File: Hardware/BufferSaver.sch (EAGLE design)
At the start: 12 parts, among them U1 SN74AHC1G125, U3 SN74AHC1G125

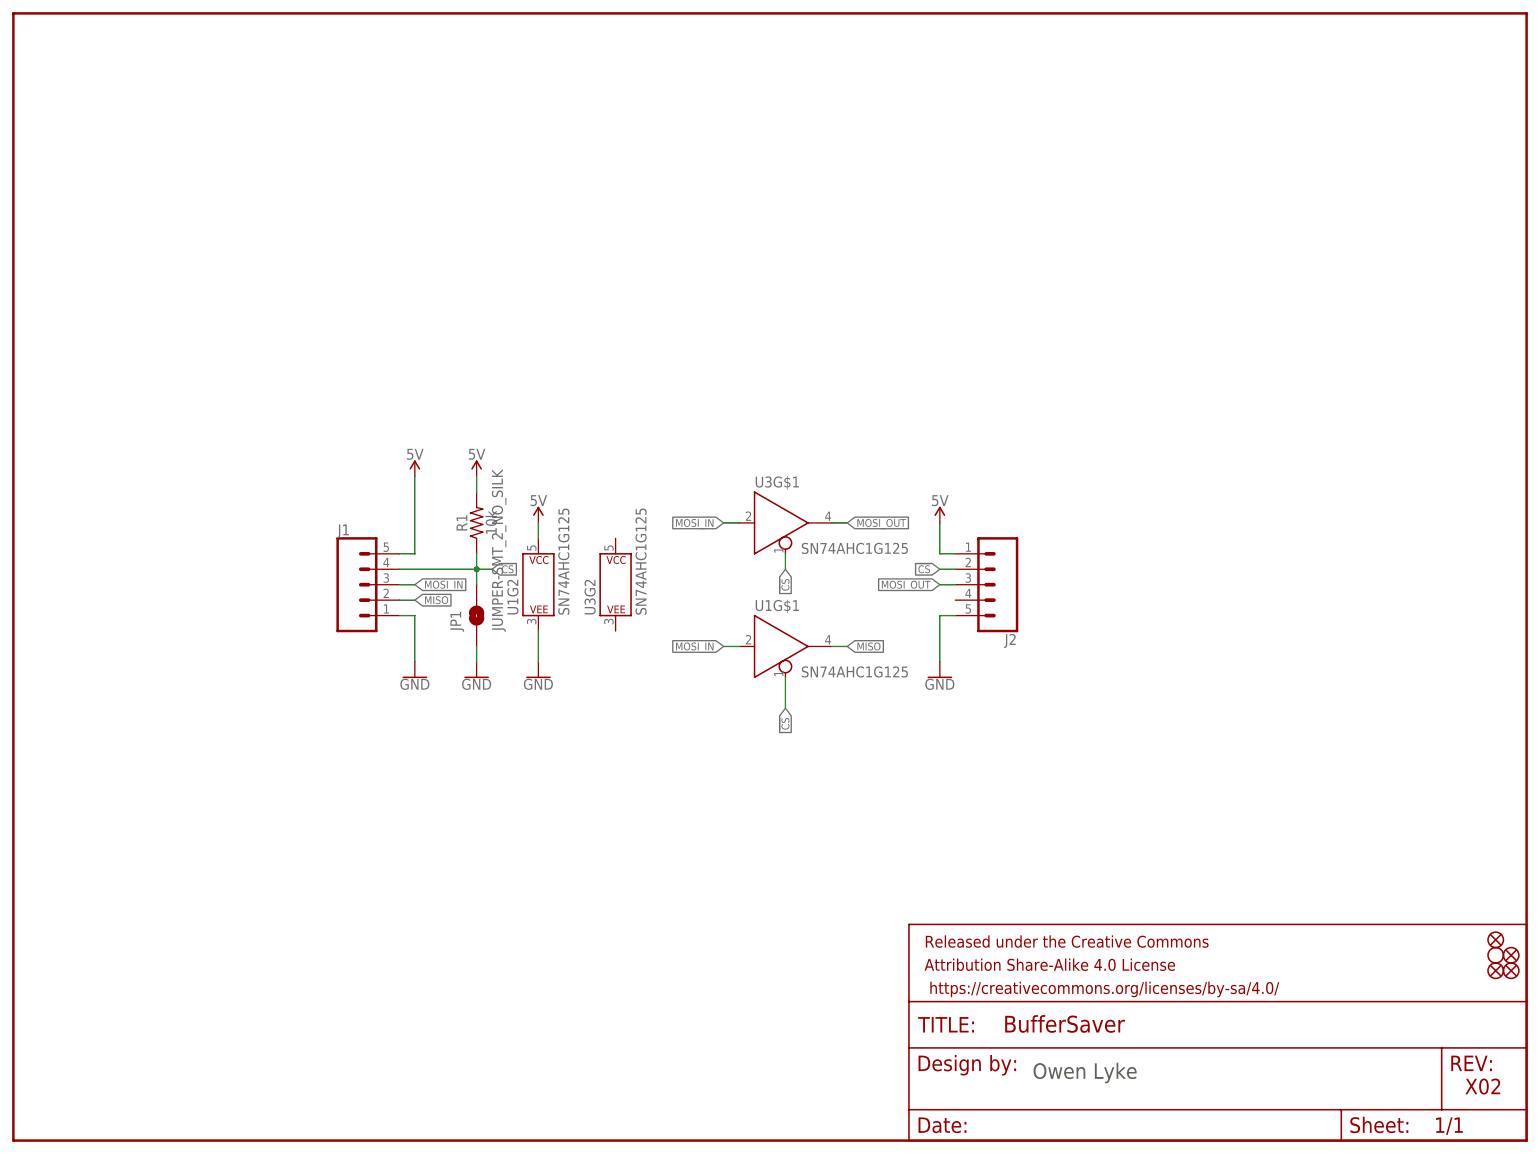
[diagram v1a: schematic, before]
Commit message: Revert "Added a second buffer to allow for multiple led strips on one SPI port!"
This reverts commit a22a5d977a95e097da70702a3350ebab49920d41.
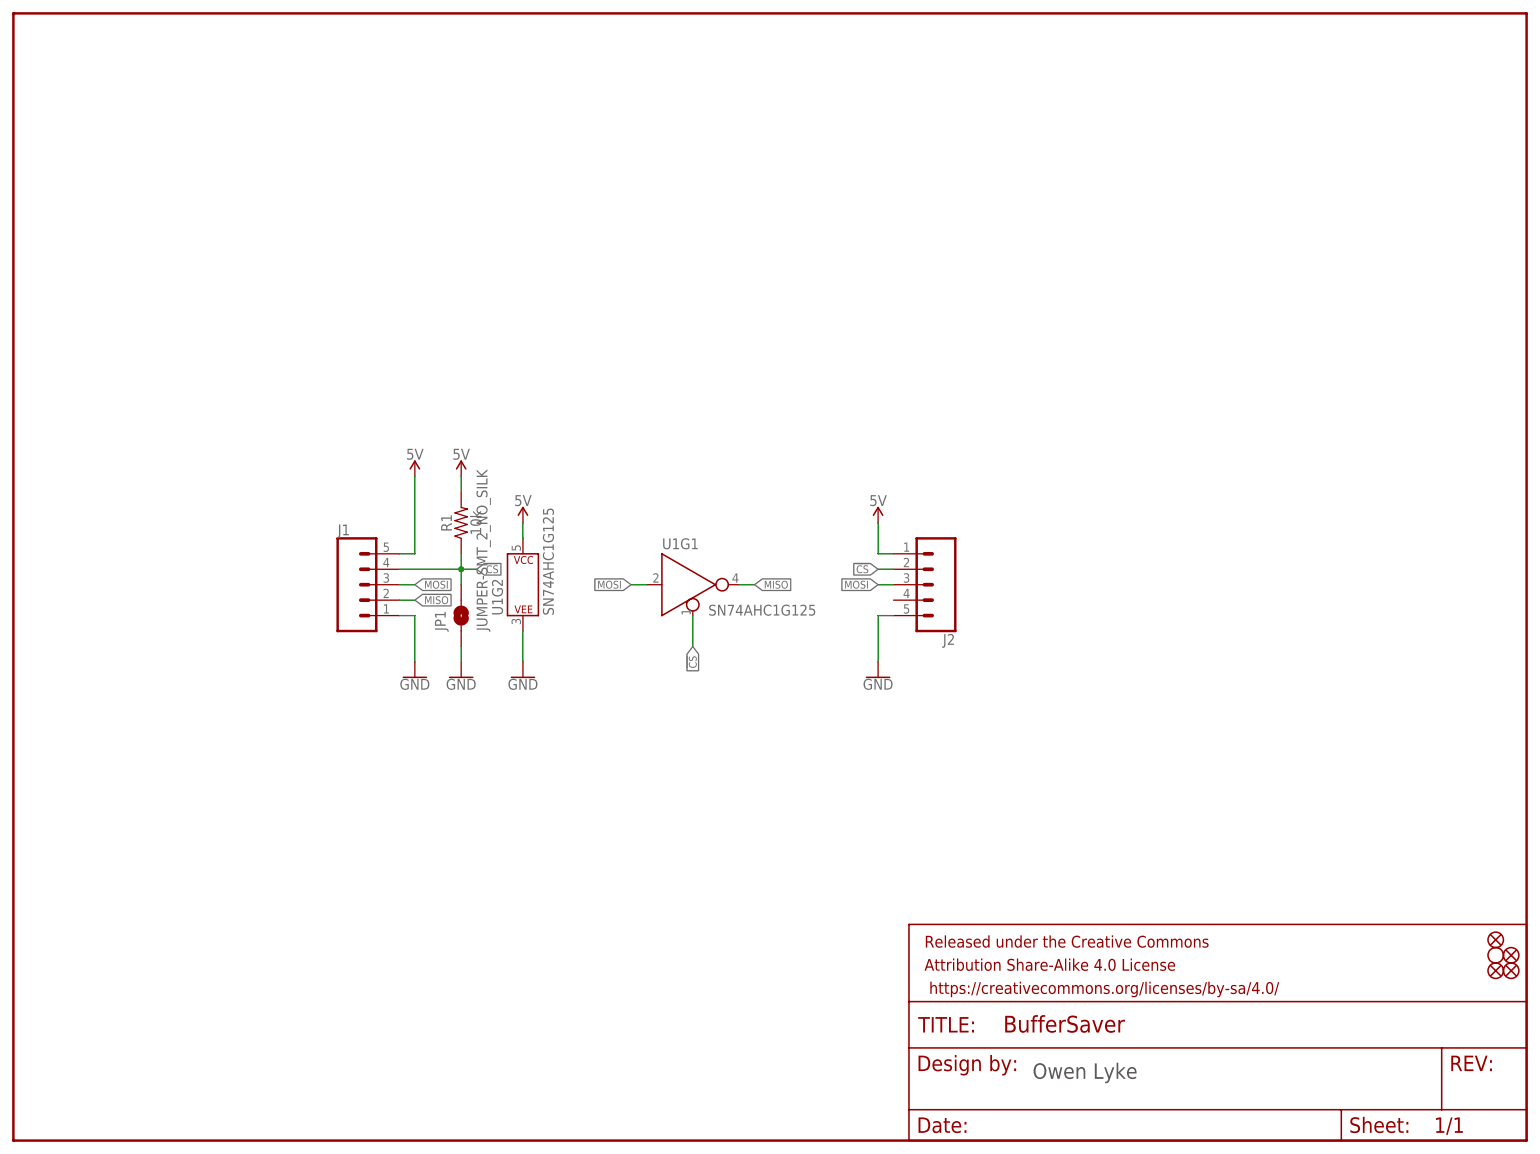
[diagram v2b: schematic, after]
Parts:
- removed U3: SN74AHC1G125, SparkFun-IC-Logic:74AHC1G125D
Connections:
- removed net MOSI_IN: J1.3, U1G$1.A, U3G$1.A
- removed net MOSI_OUT: J2.3, U3G$1.Y
- new net MOSI: J1.3, J2.3, U1G1.A
- net !CS: now also U1G1.!EN; no longer U1G$1.!EN, U3G$1.!EN
- net MISO: now also U1G1.Y; no longer U1G$1.Y
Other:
- note removed: "X02"
- moved on the sheet: J2, JP1, R1, U1G2
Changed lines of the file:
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@@
 <?xml version="1.0" encoding="utf-8"?>
 <!DOCTYPE eagle SYSTEM "eagle.dtd">
-<eagle version="9.1.3">
+<eagle version="9.0.1">
 <drawing>
 <settings>
@@
 <part name="JP1" library="SparkFun-Jumpers" deviceset="JUMPER-SMT_2_NO" device="_SILK"/>
 <part name="GND4" library="SparkFun-PowerSymbols" deviceset="GND" device=""/>
-<part name="U3" library="SparkFun-IC-Logic" deviceset="74*1G125" device="D" technology="AHC" value="SN74AHC1G125"/>
 </parts>
 <sheets>
@@
 <plain>
 <text x="68.58" y="-81.28" size="2.54" layer="97">Owen Lyke</text>
-<text x="139.7" y="-83.82" size="2.54" layer="94">X02</text>
 </plain>
 <instances>
+<instance part="U1" gate="G1" x="10.16" y="0"/>
 <instance part="J1" gate="G$1" x="-43.18" y="0"/>
-<instance part="J2" gate="G$1" x="63.5" y="0" rot="R180"/>
+<instance part="J2" gate="G$1" x="53.34" y="0" rot="R180"/>
 <instance part="SUPPLY1" gate="G$1" x="-33.02" y="17.78"/>
-<instance part="SUPPLY2" gate="G$1" x="53.34" y="10.16"/>
+<instance part="SUPPLY2" gate="G$1" x="43.18" y="10.16"/>
 <instance part="GND1" gate="1" x="-33.02" y="-15.24"/>
-<instance part="GND2" gate="1" x="53.34" y="-15.24"/>
+<instance part="GND2" gate="1" x="43.18" y="-15.24"/>
 <instance part="FRAME1" gate="G$1" x="-99.06" y="-91.44"/>
 <instance part="FRAME1" gate="V" x="48.26" y="-91.44"/>
@@
 <instance part="FD1" gate="G$1" x="144.78" y="-58.42"/>
 <instance part="FD2" gate="G$1" x="147.32" y="-60.96"/>
-<instance part="U1" gate="G2" x="-12.7" y="0"/>
-<instance part="SUPPLY3" gate="G$1" x="-12.7" y="10.16"/>
-<instance part="GND3" gate="1" x="-12.7" y="-15.24"/>
+<instance part="U1" gate="G2" x="-15.24" y="0"/>
+<instance part="SUPPLY3" gate="G$1" x="-15.24" y="10.16"/>
+<instance part="GND3" gate="1" x="-15.24" y="-15.24"/>
 <instance part="FD3" gate="G$1" x="144.78" y="-63.5"/>
 <instance part="FD4" gate="G$1" x="147.32" y="-63.5"/>
-<instance part="R1" gate="G$1" x="-22.86" y="10.16" rot="R90"/>
-<instance part="SUPPLY4" gate="G$1" x="-22.86" y="17.78"/>
-<instance part="JP1" gate="G$1" x="-22.86" y="-5.08" rot="R90"/>
-<instance part="GND4" gate="1" x="-22.86" y="-15.24"/>
-<instance part="U3" gate="G2" x="0" y="0"/>
-<instance part="U1" gate="G$1" x="25.4" y="-10.16"/>
-<instance part="U3" gate="G$1" x="25.4" y="10.16"/>
+<instance part="R1" gate="G$1" x="-25.4" y="10.16" rot="R90"/>
+<instance part="SUPPLY4" gate="G$1" x="-25.4" y="17.78"/>
+<instance part="JP1" gate="G$1" x="-25.4" y="-5.08" rot="R90"/>
+<instance part="GND4" gate="1" x="-25.4" y="-15.24"/>
 </instances>
 <busses>
@@
 <segment>
 <pinref part="J2" gate="G$1" pin="5"/>
-<wire x1="55.88" y1="-5.08" x2="53.34" y2="-5.08" width="0.1524" layer="91"/>
+<wire x1="45.72" y1="-5.08" x2="43.18" y2="-5.08" width="0.1524" layer="91"/>
 <pinref part="GND2" gate="1" pin="GND"/>
-<wire x1="53.34" y1="-5.08" x2="53.34" y2="-12.7" width="0.1524" layer="91"/>
+<wire x1="43.18" y1="-5.08" x2="43.18" y2="-12.7" width="0.1524" layer="91"/>
 </segment>
 <segment>
 <pinref part="U1" gate="G2" pin="P$V-"/>
-<wire x1="-12.7" y1="-7.62" x2="-12.7" y2="-12.7" width="0.1524" layer="91"/>
+<wire x1="-15.24" y1="-7.62" x2="-15.24" y2="-12.7" width="0.1524" layer="91"/>
 <pinref part="GND3" gate="1" pin="GND"/>
 </segment>
@@
 <pinref part="GND4" gate="1" pin="GND"/>
 <pinref part="JP1" gate="G$1" pin="1"/>
-<wire x1="-22.86" y1="-12.7" x2="-22.86" y2="-10.16" width="0.1524" layer="91"/>
+<wire x1="-25.4" y1="-12.7" x2="-25.4" y2="-10.16" width="0.1524" layer="91"/>
 </segment>
 </net>
@@
 <segment>
 <pinref part="J2" gate="G$1" pin="1"/>
-<wire x1="55.88" y1="5.08" x2="53.34" y2="5.08" width="0.1524" layer="91"/>
+<wire x1="45.72" y1="5.08" x2="43.18" y2="5.08" width="0.1524" layer="91"/>
 <pinref part="SUPPLY2" gate="G$1" pin="5V"/>
-<wire x1="53.34" y1="5.08" x2="53.34" y2="10.16" width="0.1524" layer="91"/>
+<wire x1="43.18" y1="5.08" x2="43.18" y2="10.16" width="0.1524" layer="91"/>
 </segment>
 <segment>
 <pinref part="U1" gate="G2" pin="P$V+"/>
-<wire x1="-12.7" y1="7.62" x2="-12.7" y2="10.16" width="0.1524" layer="91"/>
+<wire x1="-15.24" y1="7.62" x2="-15.24" y2="10.16" width="0.1524" layer="91"/>
 <pinref part="SUPPLY3" gate="G$1" pin="5V"/>
 </segment>
 <segment>
 <pinref part="R1" gate="G$1" pin="2"/>
-<wire x1="-22.86" y1="15.24" x2="-22.86" y2="17.78" width="0.1524" layer="91"/>
+<wire x1="-25.4" y1="15.24" x2="-25.4" y2="17.78" width="0.1524" layer="91"/>
 <pinref part="SUPPLY4" gate="G$1" pin="5V"/>
 </segment>
@@
 <segment>
 <pinref part="J1" gate="G$1" pin="4"/>
-<wire x1="-35.56" y1="2.54" x2="-22.86" y2="2.54" width="0.1524" layer="91"/>
-<label x="-20.32" y="2.54" size="1.27" layer="95" xref="yes"/>
+<wire x1="-35.56" y1="2.54" x2="-25.4" y2="2.54" width="0.1524" layer="91"/>
+<label x="-22.86" y="2.54" size="1.27" layer="95" xref="yes"/>
 <pinref part="R1" gate="G$1" pin="1"/>
-<wire x1="-22.86" y1="2.54" x2="-20.32" y2="2.54" width="0.1524" layer="91"/>
-<wire x1="-22.86" y1="5.08" x2="-22.86" y2="2.54" width="0.1524" layer="91"/>
-<junction x="-22.86" y="2.54"/>
+<wire x1="-25.4" y1="2.54" x2="-22.86" y2="2.54" width="0.1524" layer="91"/>
+<wire x1="-25.4" y1="5.08" x2="-25.4" y2="2.54" width="0.1524" layer="91"/>
+<junction x="-25.4" y="2.54"/>
 <pinref part="JP1" gate="G$1" pin="2"/>
-<wire x1="-22.86" y1="0" x2="-22.86" y2="2.54" width="0.1524" layer="91"/>
+<wire x1="-25.4" y1="0" x2="-25.4" y2="2.54" width="0.1524" layer="91"/>
 </segment>
 <segment>
 <pinref part="J2" gate="G$1" pin="2"/>
-<wire x1="55.88" y1="2.54" x2="53.34" y2="2.54" width="0.1524" layer="91"/>
-<label x="53.34" y="2.54" size="1.27" layer="95" rot="R180" xref="yes"/>
-</segment>
-<segment>
-<wire x1="27.94" y1="-15.24" x2="27.94" y2="-20.32" width="0.1524" layer="91"/>
-<label x="27.94" y="-20.32" size="1.27" layer="95" rot="R270" xref="yes"/>
-<pinref part="U1" gate="G$1" pin="!EN"/>
-</segment>
-<segment>
-<pinref part="U3" gate="G$1" pin="!EN"/>
-<wire x1="27.94" y1="2.54" x2="27.94" y2="5.08" width="0.1524" layer="91"/>
-<label x="27.94" y="2.54" size="1.27" layer="95" rot="R270" xref="yes"/>
-</segment>
-</net>
-<net name="MOSI_IN" class="0">
+<wire x1="45.72" y1="2.54" x2="43.18" y2="2.54" width="0.1524" layer="91"/>
+<label x="43.18" y="2.54" size="1.27" layer="95" rot="R180" xref="yes"/>
+</segment>
+<segment>
+<pinref part="U1" gate="G1" pin="!EN"/>
+<wire x1="12.7" y1="-5.08" x2="12.7" y2="-10.16" width="0.1524" layer="91"/>
+<label x="12.7" y="-10.16" size="1.27" layer="95" rot="R270" xref="yes"/>
+</segment>
+</net>
+<net name="MOSI" class="0">
 <segment>
 <pinref part="J1" gate="G$1" pin="3"/>
@@
 </segment>
 <segment>
-<wire x1="20.32" y1="-10.16" x2="17.78" y2="-10.16" width="0.1524" layer="91"/>
-<label x="17.78" y="-10.16" size="1.27" layer="95" rot="R180" xref="yes"/>
-<pinref part="U1" gate="G$1" pin="A"/>
-</segment>
-<segment>
-<pinref part="U3" gate="G$1" pin="A"/>
-<wire x1="20.32" y1="10.16" x2="17.78" y2="10.16" width="0.1524" layer="91"/>
-<label x="17.78" y="10.16" size="1.27" layer="95" rot="R180" xref="yes"/>
+<pinref part="U1" gate="G1" pin="A"/>
+<wire x1="5.08" y1="0" x2="2.54" y2="0" width="0.1524" layer="91"/>
+<label x="2.54" y="0" size="1.27" layer="95" rot="R180" xref="yes"/>
+</segment>
+<segment>
+<pinref part="J2" gate="G$1" pin="3"/>
+<wire x1="45.72" y1="0" x2="43.18" y2="0" width="0.1524" layer="91"/>
+<label x="43.18" y="0" size="1.27" layer="95" rot="R180" xref="yes"/>
 </segment>
 </net>
 <net name="MISO" class="0">
 <segment>
-<wire x1="35.56" y1="-10.16" x2="38.1" y2="-10.16" width="0.1524" layer="91"/>
-<label x="38.1" y="-10.16" size="1.27" layer="95" xref="yes"/>
-<pinref part="U1" gate="G$1" pin="Y"/>
+<pinref part="U1" gate="G1" pin="Y"/>
+<wire x1="20.32" y1="0" x2="22.86" y2="0" width="0.1524" layer="91"/>
+<label x="22.86" y="0" size="1.27" layer="95" xref="yes"/>
 </segment>
 <segment>
@@
 </segment>
 </net>
-<net name="MOSI_OUT" class="0">
-<segment>
-<pinref part="U3" gate="G$1" pin="Y"/>
-<wire x1="38.1" y1="10.16" x2="35.56" y2="10.16" width="0.1524" layer="91"/>
-<label x="38.1" y="10.16" size="1.27" layer="95" xref="yes"/>
-</segment>
-<segment>
-<pinref part="J2" gate="G$1" pin="3"/>
-<wire x1="55.88" y1="0" x2="53.34" y2="0" width="0.1524" layer="91"/>
-<label x="53.34" y="0" size="1.27" layer="95" rot="R180" xref="yes"/>
-</segment>
-</net>
